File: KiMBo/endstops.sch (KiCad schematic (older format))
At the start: 32 parts

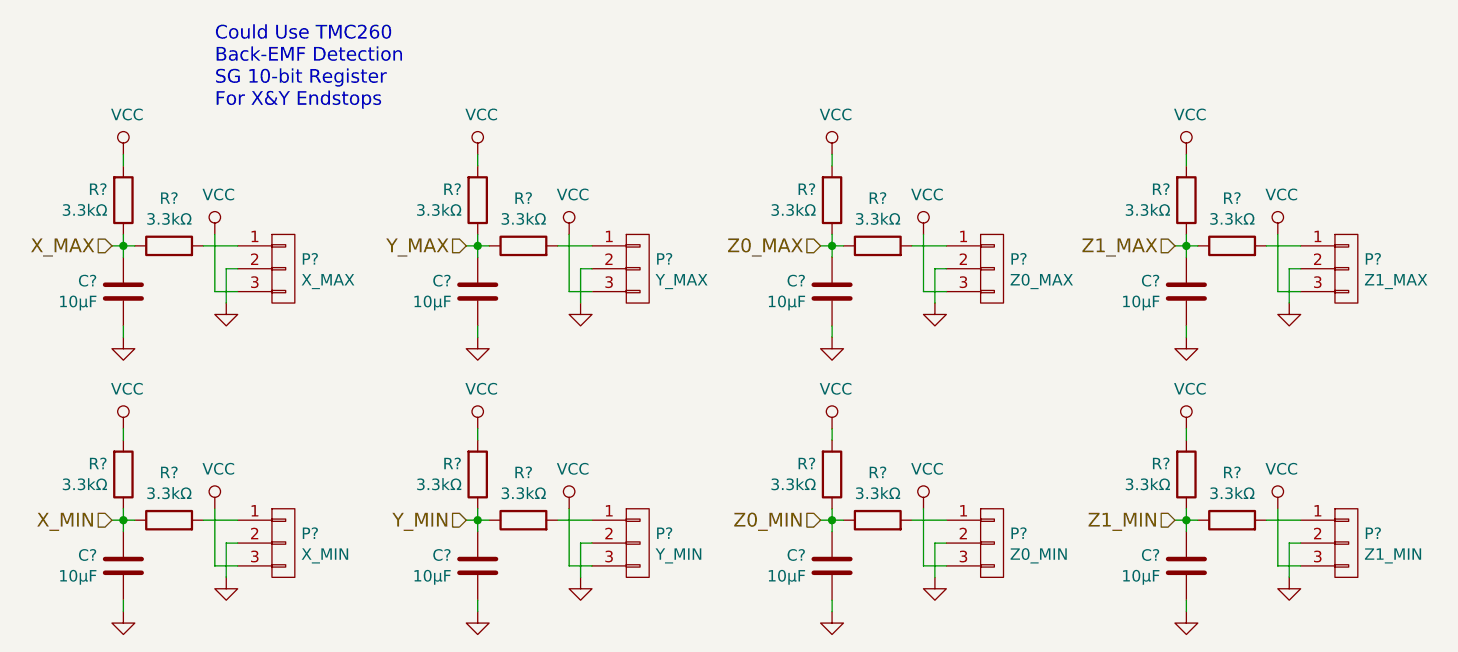
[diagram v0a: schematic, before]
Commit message: Add eMMC to the schematic
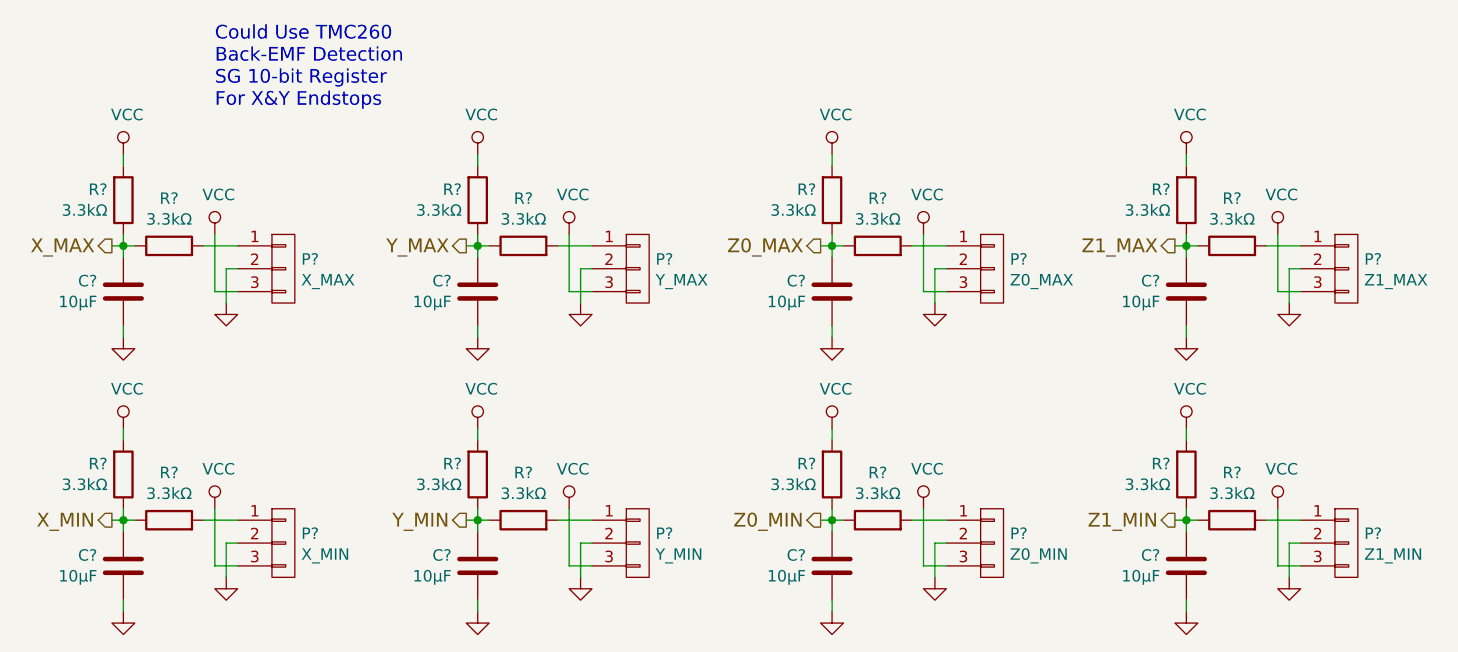
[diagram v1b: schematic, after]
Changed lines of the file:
@@
 LIBS:KiMBo
 LIBS:KiMBo-cache
-EELAYER 25 0
+EELAYER 26 0
 EELAYER END
 $Descr A3 16535 11693
 encoding utf-8
-Sheet 7 20
+Sheet 18 18
 Title ""
 Date ""
@@
 	1    0    0    -1
 $EndComp
-Text HLabel 1900 3150 0    60   Input ~ 0
+Text HLabel 1900 3150 0    60   Output ~ 0
 X_MAX
 $Comp
@@
 	1    0    0    -1
 $EndComp
-Text HLabel 1900 4350 0    60   Input ~ 0
+Text HLabel 1900 4350 0    60   Output ~ 0
 X_MIN
 $Comp
@@
 	1    0    0    -1
 $EndComp
-Text HLabel 3450 3150 0    60   Input ~ 0
+Text HLabel 3450 3150 0    60   Output ~ 0
 Y_MAX
 $Comp
@@
 	1    0    0    -1
 $EndComp
-Text HLabel 3450 4350 0    60   Input ~ 0
+Text HLabel 3450 4350 0    60   Output ~ 0
 Y_MIN
 $Comp
@@
 	1    0    0    -1
 $EndComp
-Text HLabel 5000 3150 0    60   Input ~ 0
+Text HLabel 5000 3150 0    60   Output ~ 0
 Z0_MAX
 $Comp
@@
 	1    0    0    -1
 $EndComp
-Text HLabel 5000 4350 0    60   Input ~ 0
+Text HLabel 5000 4350 0    60   Output ~ 0
 Z0_MIN
 $Comp
@@
 	1    0    0    -1
 $EndComp
-Text HLabel 6550 3150 0    60   Input ~ 0
+Text HLabel 6550 3150 0    60   Output ~ 0
 Z1_MAX
 $Comp
@@
 	1    0    0    -1
 $EndComp
-Text HLabel 6550 4350 0    60   Input ~ 0
+Text HLabel 6550 4350 0    60   Output ~ 0
 Z1_MIN
 $Comp
